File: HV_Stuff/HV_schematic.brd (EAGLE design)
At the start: 100 x 80 mm, 7 parts

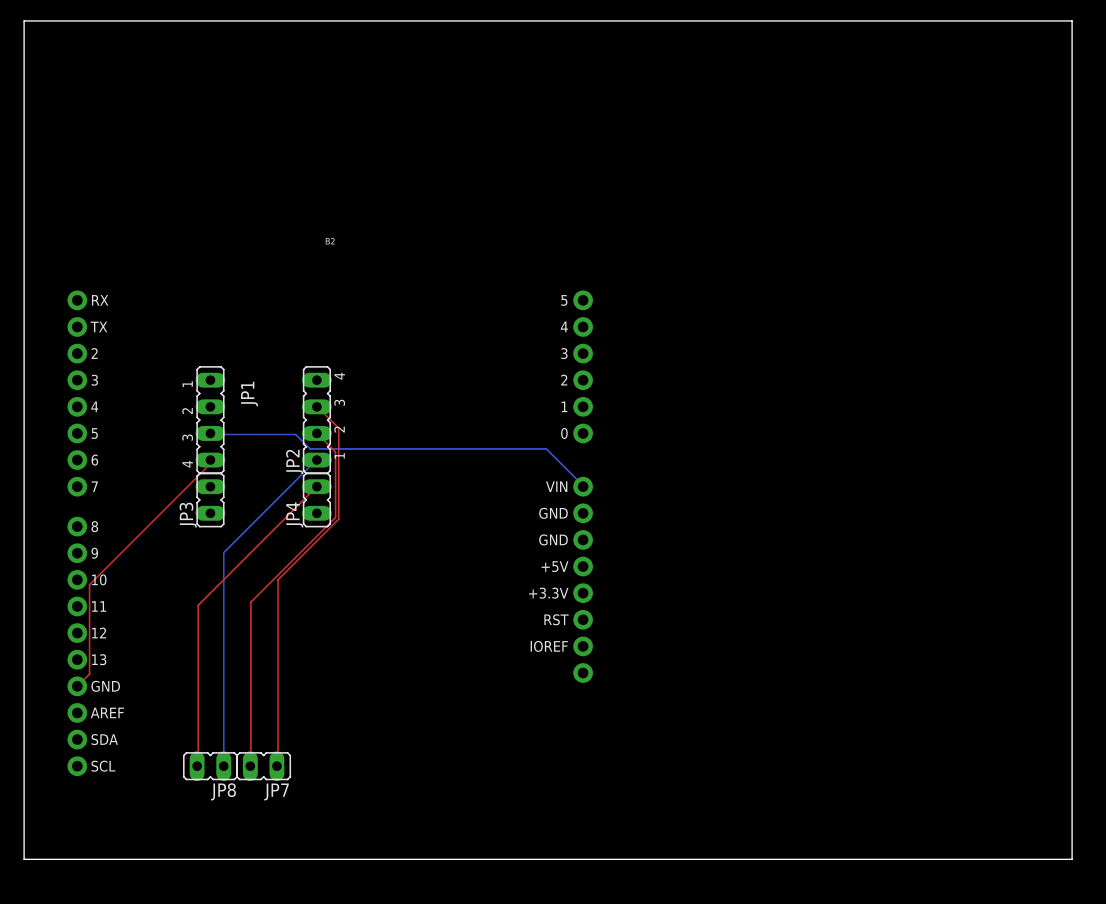
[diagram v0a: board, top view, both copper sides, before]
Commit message: Changed to mega
Got schematic and PCB running on a mega
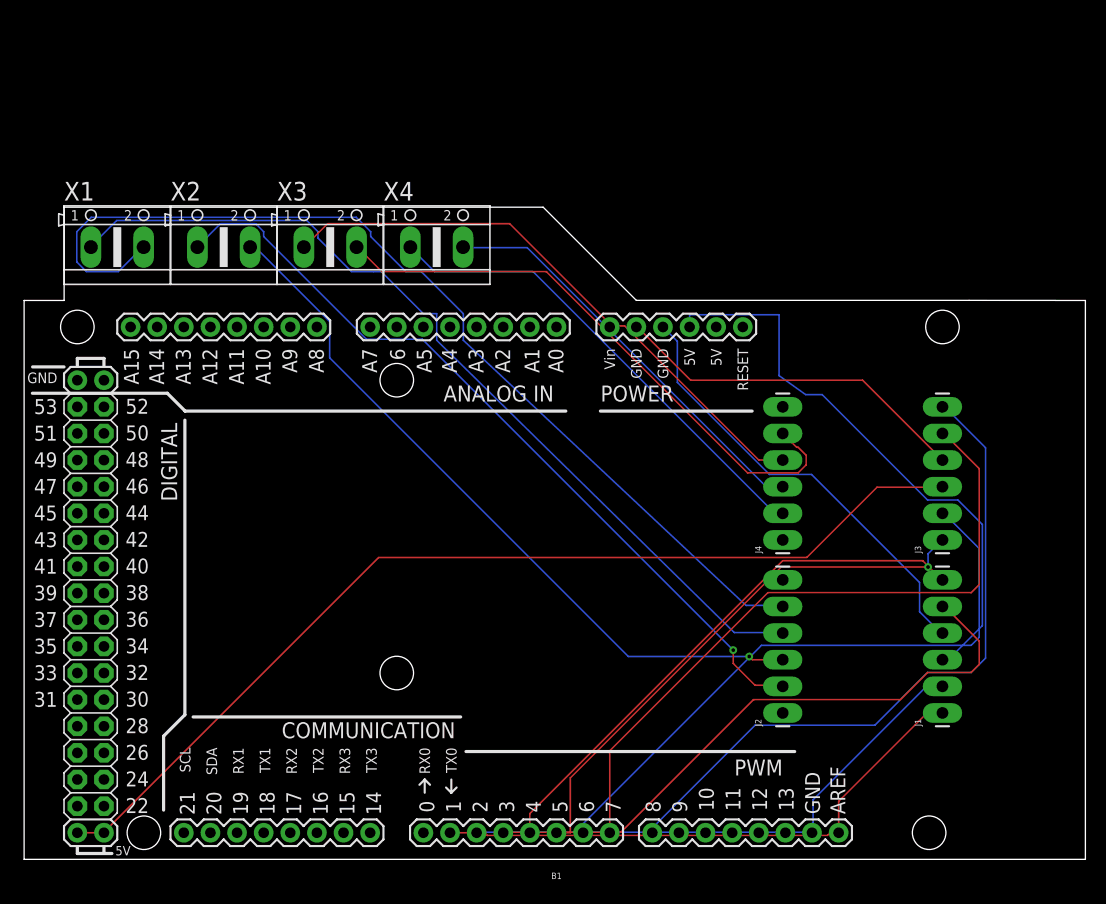
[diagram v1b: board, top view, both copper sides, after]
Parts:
- removed B2: ARDUINO_UNO_R3_SHIELDBASIC, SparkFun-Boards:UNO_R3_SHIELD
- removed JP1, JP2: (no value), jumper:JP4
- removed JP3, JP4, JP7, JP8: (no value), jumper:JP1
- added B1: ARDUINO_MEGA_R3FULL, SparkFun-Boards:ARDUINO_MEGA
- added J1, J2, J3, J4: (no value), SparkFun-Connectors:1X06_LONGPADS
- added X1, X2, X3, X4: (no value), con-ptr500:AK500/2
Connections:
- new net GND2: B1.GND@1, J3.4
- new net IN1_2: B1.5, J3.1
- new net IN2_2: B1.6, J3.2
- new net IN3_2: B1.7, J3.5
- new net IN4_2: B1.8, J3.6
- new net OUT1_2: J4.5, X3.2
- new net OUT2_2: J4.4, X3.1
- new net OUT3_2: J4.3, X4.2
- new net OUT4_2: J4.2, X4.1
- new net VCC2: B1.5V@1, B1.5V@2, J3.3
- net GND: now also B1.GND@0, J1.4; no longer B2.GND@2, JP1.4
- net IN1: now also B1.1, J1.1; no longer JP3.2
- net IN2: now also B1.2, J1.2; no longer JP3.1
- net IN3: now also B1.3, J1.5; no longer JP1.2
- net IN4: now also B1.4, J1.6; no longer JP1.1
- net OUT1: now also J2.5, X1.2; no longer JP2.3, JP7.1
- net OUT2: now also J2.4, X1.1; no longer JP2.2, JP7.2
- net OUT3: now also J2.3, X2.2; no longer JP2.1, JP8.1
- net OUT4: now also J2.2, X2.1; no longer JP4.2, JP8.2
- net VCC: now also B1.5V@0, J1.3; no longer B2.VIN, JP1.3
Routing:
- net VCC2: track 0.00 -> 96.3 mm
- net IN3_2: track 0.00 -> 65.6 mm
- net IN4_2: track 0.00 -> 64.9 mm
- net IN2_2: track 0.00 -> 59.4 mm
- net IN3: track 0.00 -> 59.3 mm
- net OUT1: track 37.6 -> 95.2 mm
- net OUT1_2: track 0.00 -> 56.1 mm
- net OUT2_2: track 0.00 -> 56.0 mm
- net IN1: track 0.00 -> 53.2 mm
- net IN1_2: track 0.00 -> 52.2 mm, vias 0 -> 1
- net IN4: track 0.00 -> 52.0 mm
- net IN2: track 0.00 -> 51.5 mm
- net OUT2: track 35.8 -> 85.1 mm
- net OUT4_2: track 0.00 -> 46.1 mm
- net OUT4: track 31.4 -> 76.1 mm, vias 0 -> 1
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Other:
- board size 100 x 80 mm -> 101.3 x 62.2 mm

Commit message: Made it, it's gorgeous. It looks very pretty
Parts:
- removed X1, X2, X3, X4: (no value), con-ptr500:AK500/2
- added M1, M2, M3, M4: (no value), con-ptr500:AK500/2
- B1: device SparkFun-Boards:ARDUINO_MEGA -> Will Library:ARDUINO_MEGA
- moved J3 82.6 mm to (5.08, 27.9)
- moved J4 52.1 mm to (20.3, 27.9)
- moved J1 35.1 mm to (61.0, 36.8), turned to 180 degrees
- moved B1 24.1 mm to (27.9, 26.7), turned to 0 degrees
- moved J2 13.7 mm to (61.0, 21.6), turned to 180 degrees
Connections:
- net IN1 renamed IN1_1
- net IN2 renamed IN2_1
- net IN3 renamed IN3_1
- net IN4 renamed IN4_1
- removed net GND: B1.GND@0, J1.4
- removed net GND2: B1.GND@1, J3.4
- removed net OUT1: J2.5, X1.2
- removed net OUT2: J2.4, X1.1
- removed net OUT3: J2.3, X2.2
- removed net OUT4: J2.2, X2.1
- removed net VCC: B1.5V@0, J1.3
- removed net VCC2: B1.5V@1, B1.5V@2, J3.3
- new net 5V_1: B1.5V@2, J1.3
- new net 5V_2: B1.5V@0, J3.3
- new net GND_1: B1.GND@3, J1.4
- new net GND_2: B1.GND@4, J3.4
- new net N$1: J2.3, M2.1
- new net OUT1_1: J2.5, M1.1
- new net OUT2_1: J2.4, M1.2
- new net OUT4_1: J2.2, M2.2
- net OUT1_2: now also M3.1; no longer X3.2
- net OUT2_2: now also M3.2; no longer X3.1
- net OUT3_2: now also M4.1; no longer X4.2
- net OUT4_2: now also M4.2; no longer X4.1
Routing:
- net VCC2: track 96.3 -> 0.00 mm
- net OUT1: track 95.2 -> 0.00 mm
- net OUT2: track 85.1 -> 0.00 mm
- net OUT4: track 76.1 -> 0.00 mm, vias 1 -> 0
- net OUT3: track 69.2 -> 0.00 mm, vias 1 -> 0
- net VCC: track 55.4 -> 0.00 mm
- net GND_1: track 0.00 -> 44.1 mm
- net IN4_2: track 64.9 -> 21.6 mm
- net GND: track 42.8 -> 0.00 mm
- net IN3_2: track 65.6 -> 27.3 mm
- net 5V_2: track 0.00 -> 38.1 mm
- net OUT4_1: track 0.00 -> 37.7 mm
- net N$1: track 0.00 -> 37.5 mm
- net OUT1_1: track 0.00 -> 36.6 mm
- net OUT2_1: track 0.00 -> 36.5 mm
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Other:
- board size 101.3 x 62.2 mm -> 82.2 x 63.5 mm
